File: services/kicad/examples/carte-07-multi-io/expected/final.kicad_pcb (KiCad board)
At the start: 2 copper layers, 115 x 85 mm, 47 parts, among them J1 IN_5V, J2 SWD, J3 IO0, J4 IO1, J5 IO2, J6 IO3, U1 STM32F103C8T6, U2 AMS1117-3.3

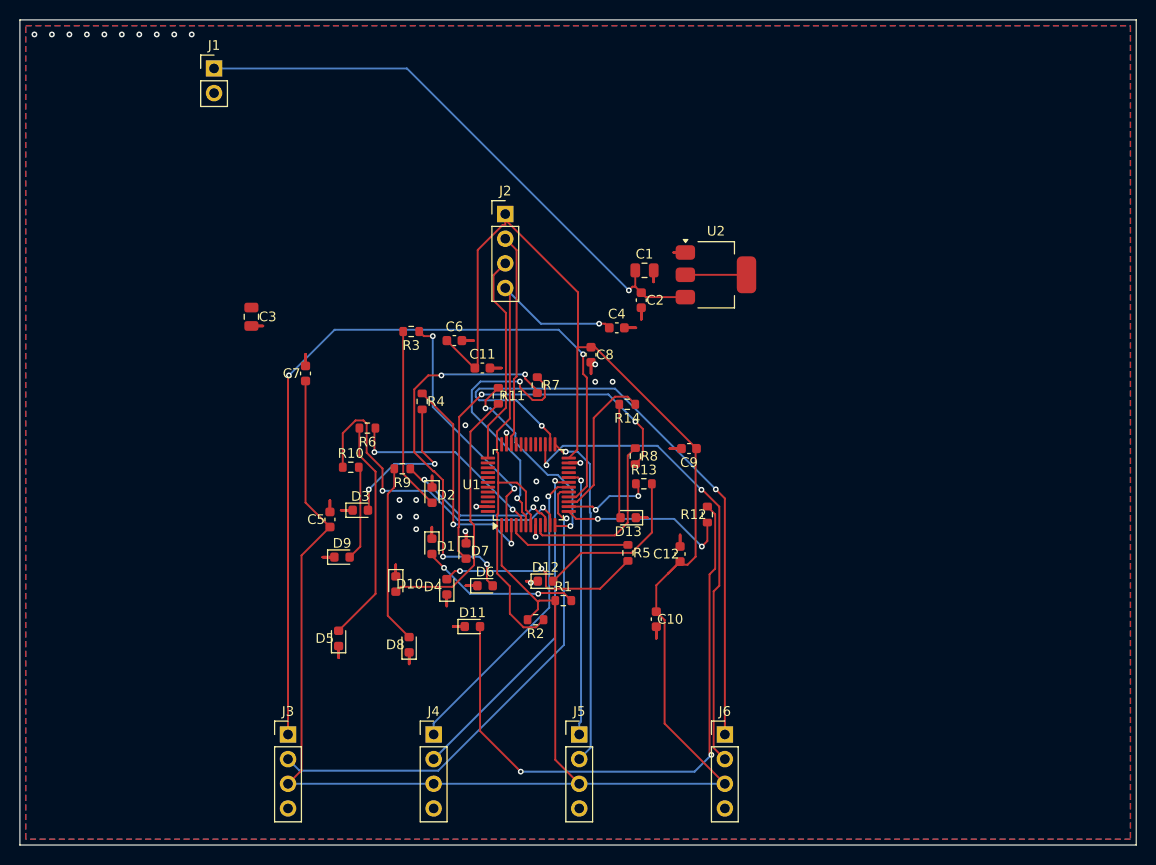
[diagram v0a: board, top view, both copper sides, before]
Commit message: test(examples): la carte 07 passe, et sa lenteur etait un tirage, pas sa taille
Elle est desormais routee a 100 %, zero connexion manquante, zero erreur de
severite `error` sur le board livre. 350 segments, 75 vias, deux couches.

Ce qui l a debloquee est le constat le plus instructif du banc.

Sa premiere version etait la carte-08 AMPUTEE de quatre paires de LED. Son
schema etait sain — verifie : aucune broche pointant vers un composant absent,
aucun composant isole, la meme structure que la carte dont elle derivait. Et
pourtant son PLACEMENT durait 1560 s, puis 70 minutes au tirage suivant, contre
104 s pour la carte-08 (56 composants) et 130 s pour la carte-10 (70). Douze a
trente fois plus long pour MOINS de composants.

J ai d abord soupconne une contention : une JVM Freerouting a 211 % de
processeur depuis sept heures, des travaux abandonnes par mes propres runs tues.
Mesure : 12 processeurs, charge moyenne 4,00, liste des sessions vide. Ce
n etait pas ca. C est le placement lui-meme, qui n a PAS de graine fixe.

Ce depot documentait deja la dispersion du placement en QUALITE — 6, 8 et 12
connexions manquantes selon le tirage. On mesure ici qu elle porte aussi sur la
DUREE, dans un rapport de trente. La duree d un pipeline ne se deduit donc pas
du nombre de composants, et un budget client calibre sur une moyenne coupera
certaines cartes en plein travail.

La carte a ete refaite en ETENDANT la carte-06, qui passe, au lieu de mutiler
la carte-08. Le placement est retombe a 662 s du premier coup, et il a fallu
deux tirages pour atteindre zero erreur — le routage est stochastique lui aussi.

Constat annexe, consigne dans docs/DECISIONS.md en attente de validation :
cinq travaux Freerouting ont tourne 996 passes chacun avec un score et un
nombre de connexions manquantes IDENTIQUES d un bout a l autre. Vingt minutes
par travail, entierement perdues, multipliees par les trois tirages de chaque
palier. Le levier serait d arreter sur absence de progression plutot que s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
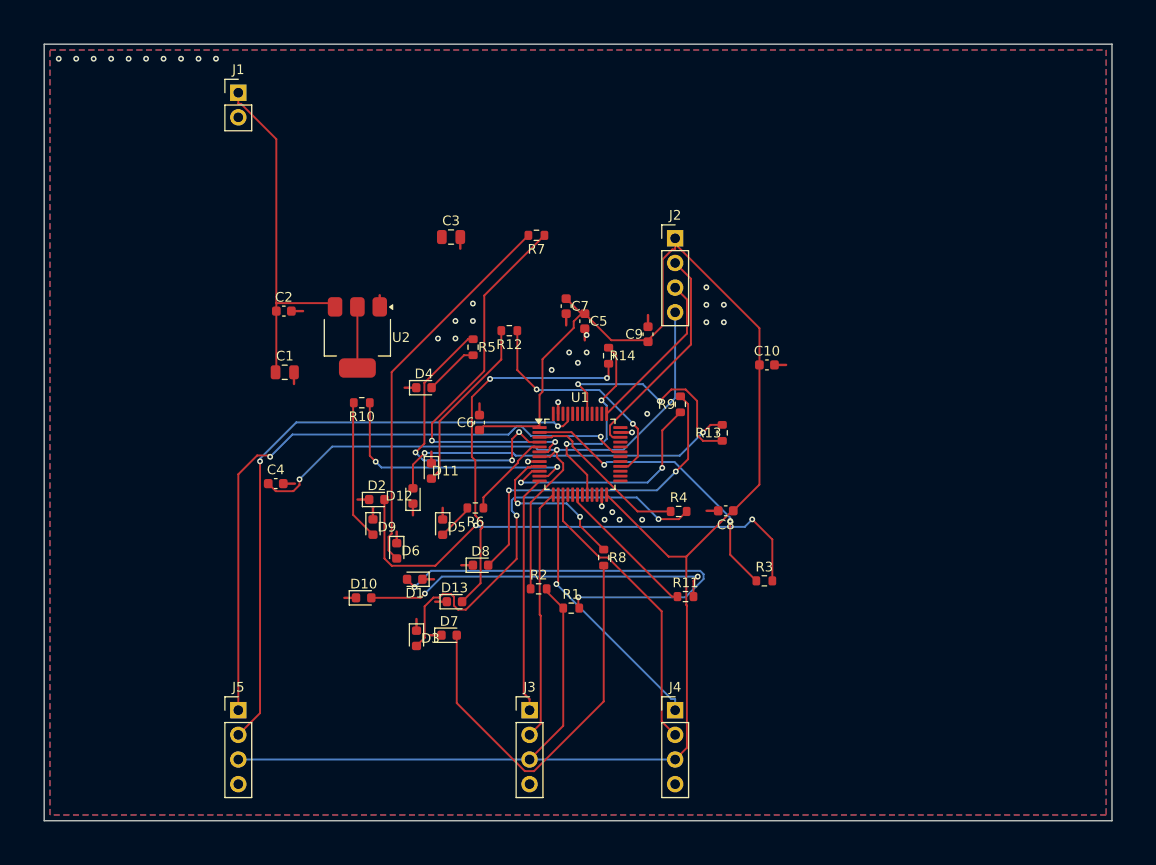
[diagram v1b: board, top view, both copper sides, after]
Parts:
- removed C11, C12: 100nF, C_0603_1608Metric
- removed J6: IO3, PinHeader_1x04_P2.54mm_Vertical
- moved R3 44.5 mm to (167.7, 120.3), turned to 0 degrees
- moved C4 38.6 mm to (117.4, 110.3)
- moved C1 38.5 mm to (118.3, 98.8)
- moved U2 37.5 mm to (125.8, 95.2), turned to -90 degrees
- moved C2 36.8 mm to (118.2, 92.5), turned to 0 degrees
- moved J5 35.2 mm to (113.5, 133.6)
- moved C5 33.3 mm to (149.2, 93.5), turned to -90 degrees
- moved R9 29.4 mm to (159.0, 102.1), turned to 90 degrees
- moved R4 28.7 mm to (158.9, 113.1), turned to 0 degrees
- moved C10 28.6 mm to (168.0, 98.0), turned to 0 degrees
- moved R11 28.3 mm to (159.6, 121.9), turned to 0 degrees
- moved R12 27.8 mm to (141.4, 94.5), turned to 180 degrees
- moved C7 27.7 mm to (147.3, 92.0), turned to -90 degrees
- moved R5 26.5 mm to (137.7, 96.2)
- moved J3 25.0 mm to (143.5, 133.6)
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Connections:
- U1 pad 12: IO_L8 -> EXT0_1
- U1 pad 13: IO_L9 -> EXT0_2
- U1 pad 14: IO_L10 -> EXT1_1
- U1 pad 15: IO_L11 -> EXT1_2
- U1 pad 16: EXT0_1 -> Net-(U1-16)
- U1 pad 17: EXT0_2 -> Net-(U1-17)
- U1 pad 18: EXT1_1 -> IO_L8
- U1 pad 19: EXT1_2 -> Net-(U1-19)
- U1 pad 20: EXT2_1 -> IO_L11
- U1 pad 25: EXT2_2 -> Net-(U1-25)
- U1 pad 26: EXT3_1 -> Net-(U1-26)
- U1 pad 27: EXT3_2 -> Net-(U1-27)
- U1 pad 28: Net-(U1-28) -> IO_L9
- U1 pad 31: Net-(U1-31) -> EXT2_1
- U1 pad 41: Net-(U1-41) -> IO_L10
- U1 pad 45: Net-(U1-45) -> EXT2_2
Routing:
- net GND: track 108.0 -> 33.6 mm, vias 27 -> 34
- net EXT3_1: track 65.6 -> 0.00 mm, vias 2 -> 0
- net EXT0_1: track 86.4 -> 24.5 mm, vias 2 -> 0
- net +3V3: track 230.3 -> 178.1 mm
- net EXT3_2: track 50.3 -> 0.00 mm, vias 2 -> 0
- net LEDA9: track 63.3 -> 18.2 mm, vias 2 -> 0
- net EXT2_1: track 27.6 -> 67.1 mm, vias 1 -> 2
- net LEDA0: track 18.9 -> 53.6 mm, vias 0 -> 2
- net LED_PWR: track 16.5 -> 47.1 mm
- net EXT2_2: track 35.3 -> 63.8 mm, vias 1 -> 2
- net LEDA1: track 16.2 -> 43.4 mm
- net LEDA11: track 11.7 -> 38.7 mm, vias 0 -> 2
- net EXT0_2: track 51.7 -> 25.8 mm, vias 1 -> 0
- net VIN: track 60.3 -> 36.8 mm, vias 1 -> 0
- net LEDA3: track 23.1 -> 3.82 mm
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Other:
- board size 115 x 85 mm -> 110 x 80 mm

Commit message: feat(kicad): placement pro et routage 100 % fabricable sur les 16 cartes -- integration sur main (#164)
Branche d'integration coupee depuis origin/main (fab2a82, PR #162) : les
fichiers cles de main etaient des instantanes de feat/placement-seed-snap-
bypass (routing.py = 7981019, placement.py = 437a8b4...). On reprend donc
l'arbre entier de cette branche (345 commits, dernier 9f48667) et on y
conserve ce que main seul apportait :
- tools/verrou_routage.py + son test : « 6,2 Go par routage » rectifie
  (0,2 Go mesure ; c'est la concurrence qui emballe la memoire) ;
- tests/test_driver_llm_resync.py ;
- CLAUDE.md, PLAN.md, DECISIONS.md : fusion a trois voies, les sections
  des deux lignes conservees (2026-09-05 conteneur/verrou, 2026-09-07
  parcours asynchrone et chaine du driver, 2026-09-09/10 lecons).
Les skills *-delegate restent supprimes (remplaces le 2026-08-30).

Contenu : banc en deux phases (placement valide puis routage gele), snap
sur les regles natives, repli GND cible, journal Freerouting incremental,
horloge sans progres, via d'echappement vers le plan principal,
serigraphie degagee ; 16 cartes livrees a 100 %, 0 erreur DRC.

Verification : pytest services/kicad 1805 passed, 16 skipped ;
pnpm type-check 8/8.


Claude-Session: https://claude.ai/code/session_01TnMqm4La2CxQHHB5K8aSSV

Co-authored-by: Claude Fable 5.1 <noreply@anthropic.com>
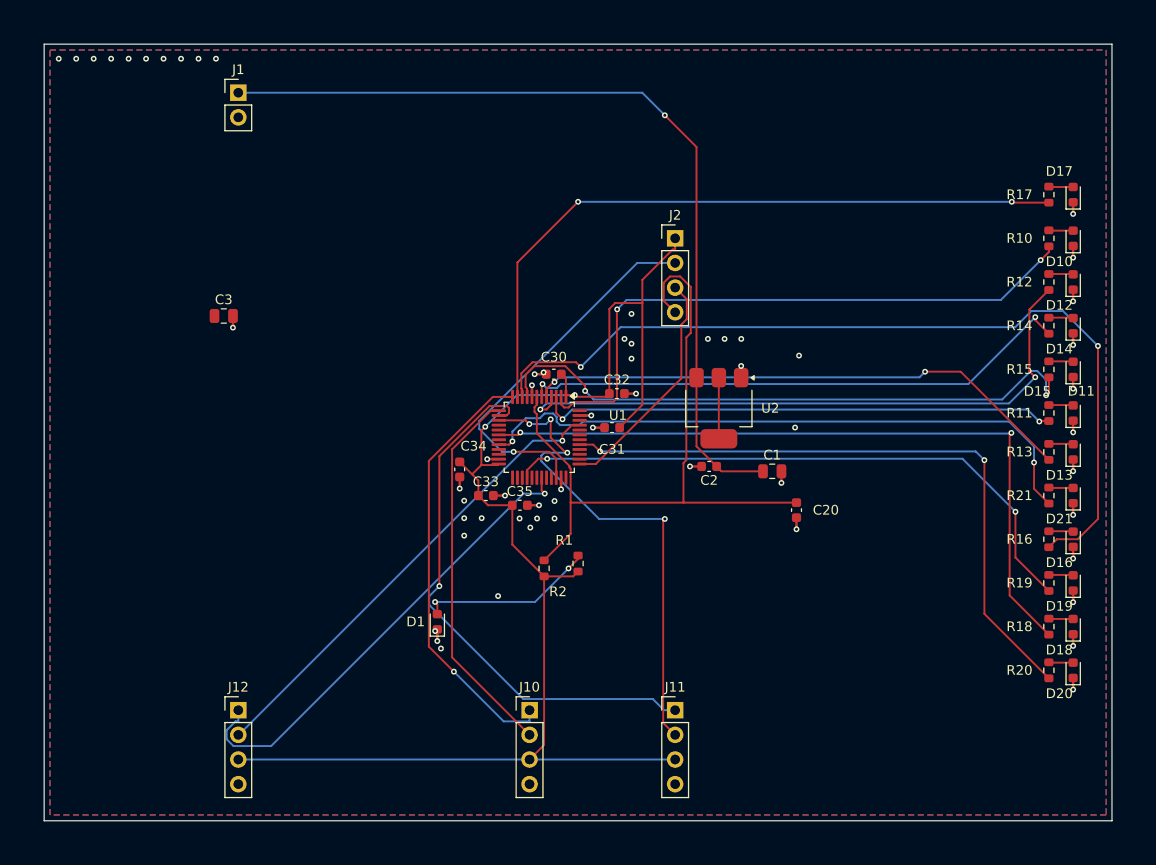
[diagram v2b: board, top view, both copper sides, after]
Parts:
- removed C10, C4, C5, C6, C7, C8, C9: 100nF, C_0603_1608Metric
- removed D2, D3, D4, D5, D6, D7, D8, D9: LED, LED_0603_1608Metric
- removed J3: IO0, PinHeader_1x04_P2.54mm_Vertical
- removed J4: IO1, PinHeader_1x04_P2.54mm_Vertical
- removed J5: IO2, PinHeader_1x04_P2.54mm_Vertical
- removed R3, R4, R5, R6, R7, R8, R9: 1k, R_0603_1608Metric
- added C20: 100nF, C_0603_1608Metric, F.Cu at (171.0, 113.0)
- added C30: 100nF, C_0603_1608Metric, F.Cu at (146.0, 99.0)
- added C31: 100nF, C_0603_1608Metric, F.Cu at (152.0, 104.5)
- added C32: 100nF, C_0603_1608Metric, F.Cu at (152.5, 101.0)
- added C33: 100nF, C_0603_1608Metric, F.Cu at (139.0, 111.5)
- added C34: 100nF, C_0603_1608Metric, F.Cu at (136.3, 108.8)
- added C35: 100nF, C_0603_1608Metric, F.Cu at (142.5, 112.5)
- added D14: LED, LED_0603_1608Metric, F.Cu at (199.5, 94.0)
- added D15: LED, LED_0603_1608Metric, F.Cu at (199.5, 98.5)
- added D16: LED, LED_0603_1608Metric, F.Cu at (199.5, 116.0)
- added D17: LED, LED_0603_1608Metric, F.Cu at (199.5, 80.5)
- added D18: LED, LED_0603_1608Metric, F.Cu at (199.5, 125.0)
- added D19: LED, LED_0603_1608Metric, F.Cu at (199.5, 120.5)
- added D20: LED, LED_0603_1608Metric, F.Cu at (199.5, 129.5)
- added D21: LED, LED_0603_1608Metric, F.Cu at (199.5, 111.5)
- added J10: IO0, PinHeader_1x04_P2.54mm_Vertical, F.Cu at (143.5, 133.6)
- added J11: IO1, PinHeader_1x04_P2.54mm_Vertical, F.Cu at (158.5, 133.6)
- added J12: IO2, PinHeader_1x04_P2.54mm_Vertical, F.Cu at (113.5, 133.6)
- added R15: 1k, R_0603_1608Metric, F.Cu at (197.0, 98.5)
- added R16: 1k, R_0603_1608Metric, F.Cu at (197.0, 116.0)
- added R17: 1k, R_0603_1608Metric, F.Cu at (197.0, 80.5)
- added R18: 1k, R_0603_1608Metric, F.Cu at (197.0, 125.0)
- added R19: 1k, R_0603_1608Metric, F.Cu at (197.0, 120.5)
- added R20: 1k, R_0603_1608Metric, F.Cu at (197.0, 129.5)
- added R21: 1k, R_0603_1608Metric, F.Cu at (197.0, 111.5)
- moved D10 81.9 mm to (199.5, 85.0), turned to 90 degrees
- moved R10 72.8 mm to (197.0, 85.0), turned to 90 degrees
- moved D12 71.5 mm to (199.5, 89.5)
- moved D11 66.4 mm to (199.5, 103.0), turned to 90 degrees
- moved D13 65.6 mm to (199.5, 107.0), turned to 90 degrees
- moved R12 55.8 mm to (197.0, 89.5), turned to 90 degrees
- moved C1 51.2 mm to (168.5, 109.0)
- moved C2 46.6 mm to (162.0, 108.5), turned to 180 degrees
- moved R14 45.5 mm to (197.0, 94.0), turned to 90 degrees
- moved R11 41.9 mm to (197.0, 103.0), turned to 90 degrees
- moved U2 37.9 mm to (163.0, 102.5)
- moved R13 33.7 mm to (197.0, 107.0)
- moved C3 24.8 mm to (112.0, 93.0)
- moved D1 4.96 mm to (134.0, 124.5), turned to 90 degrees
- moved R1 4.65 mm to (148.5, 118.5), turned to 90 degrees
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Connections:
- D10 pad 2: LEDA8 -> LEDA0
- D11 pad 2: LEDA9 -> LEDA1
- D12 pad 2: LEDA10 -> LEDA2
- D13 pad 2: LEDA11 -> LEDA3
- R10 pad 1: IO_L7 -> IO_L0
- R10 pad 2: LEDA7 -> LEDA0
- R11 pad 1: IO_L8 -> IO_L1
- R11 pad 2: LEDA8 -> LEDA1
- R12 pad 1: IO_L9 -> IO_L2
- R12 pad 2: LEDA9 -> LEDA2
- R13 pad 1: IO_L10 -> IO_L3
- R13 pad 2: LEDA10 -> LEDA3
- R14 pad 1: IO_L11 -> IO_L4
- R14 pad 2: LEDA11 -> LEDA4
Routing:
- net IO_L6: track 24.1 -> 90.5 mm
- net IO_L8: track 15.1 -> 75.5 mm, vias 0 -> 2
- net VIN: track 36.8 -> 88.3 mm, vias 0 -> 1
- net LEDA0: track 53.6 -> 2.52 mm, vias 2 -> 0
- net IO_L3: track 9.14 -> 57.1 mm, vias 0 -> 2
- net IO_L5: track 17.0 -> 63.2 mm
- net IO_L11: track 21.0 -> 65.6 mm
- net IO_L10: track 23.8 -> 67.6 mm
- net IO_L7: track 27.5 -> 71.2 mm
- net LEDA1: track 43.4 -> 2.52 mm, vias 2 -> 0
- net LEDA5: track 42.0 -> 2.52 mm
- net IO_L9: track 24.1 -> 63.4 mm
- net LEDA4: track 39.6 -> 2.52 mm
- net IO_L1: track 17.1 -> 53.6 mm, vias 0 -> 2
- net LEDA11: track 38.7 -> 2.52 mm, vias 2 -> 0
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
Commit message: test(examples): quatre cartes livrées plus petites — contour resserré mesuré sur le banc (D-2026-09-13-c A)
Banc rejoué en taille heuristique (phase 1 puis phase 2 à placement gelé) :
carte-01 25x20 -> 24,8x17 (84 % de surface), carte-04 60x45 -> 45x44,8
(75 %), carte-06 80x60 -> 65,2x59,8 (81 %), carte-07 110x80 -> 99,5x79,8
(90 %) — toutes 100 % routées, 0 erreur DRC (vérifié en local), rendus 3D
régénérés. Gain nul sur les cartes denses (le génétique remplit la carte) ;
08 et 09 non livrées (dispersion du routage, surface inchangée) ; carte-11
non livrée (carte d'escalade). Tableau complet dans docs/DECISIONS.md.

Co-Authored-By: Claude Fable 5.1 <noreply@anthropic.com>
Claude-Session: https://claude.ai/code/session_01TnMqm4La2CxQHHB5K8aSSV
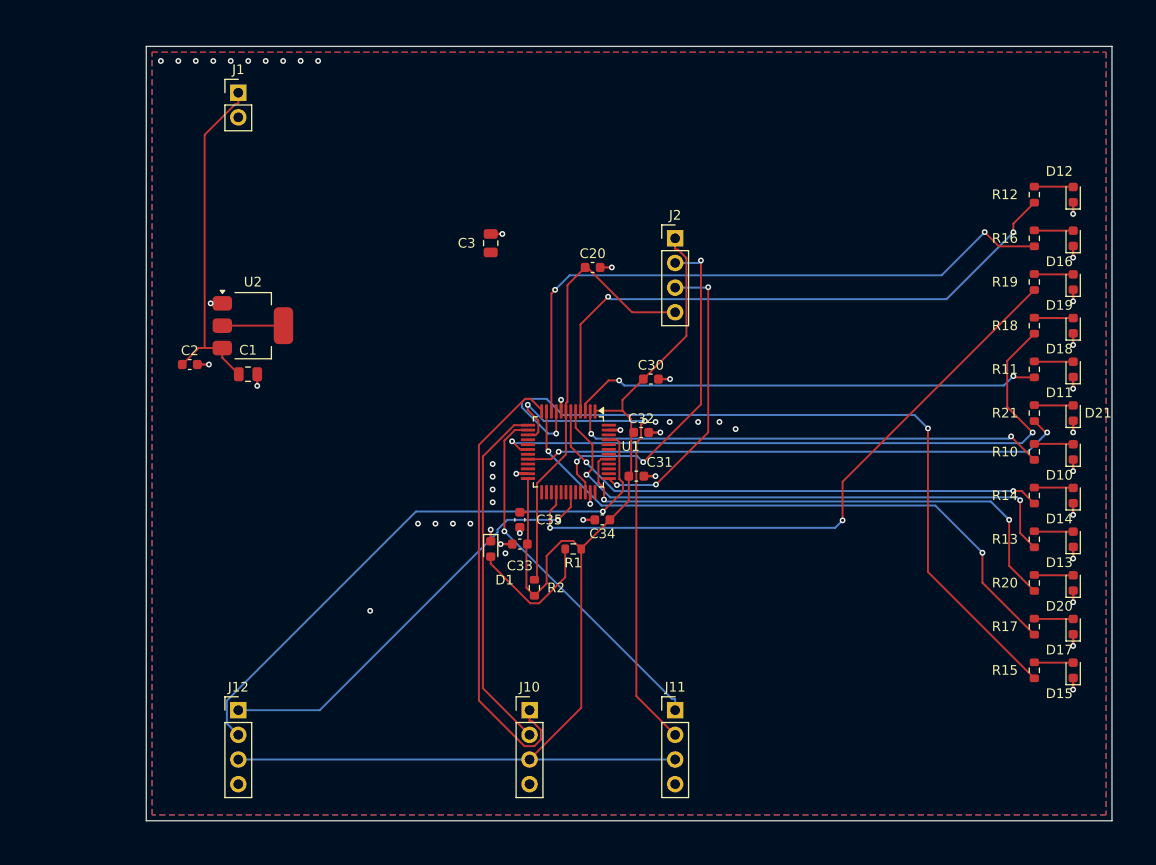
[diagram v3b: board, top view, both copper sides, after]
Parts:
- moved C1 54.9 mm to (114.5, 99.0)
- moved C2 54.5 mm to (108.5, 98.0), turned to 0 degrees
- moved U2 48.7 mm to (115.0, 94.0), turned to 0 degrees
- moved R17 44.5 mm to (195.5, 125.0)
- moved D17 44.5 mm to (199.5, 125.0)
- moved C20 32.6 mm to (150.0, 88.0), turned to 0 degrees
- moved R15 31.0 mm to (195.5, 129.5)
- moved R16 31.0 mm to (195.5, 85.0)
- moved R18 31.0 mm to (195.5, 94.0)
- moved R19 31.0 mm to (195.5, 89.5)
- moved D15 31.0 mm to (199.5, 129.5)
- moved D16 31.0 mm to (199.5, 85.0)
- moved D18 31.0 mm to (199.5, 94.0)
- moved D19 31.0 mm to (199.5, 89.5)
- moved C3 28.5 mm to (139.5, 85.5), turned to 90 degrees
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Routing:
- net VIN: track 88.3 -> 36.1 mm, vias 1 -> 0
- net NRST: track 72.4 -> 45.5 mm
- net IO_L6: track 90.5 -> 65.1 mm
- net EXT1_1: track 56.6 -> 38.1 mm
- net IO_L5: track 63.2 -> 81.0 mm
- net IO_L0: track 63.7 -> 49.3 mm
- net +3V3: track 144.5 -> 132.4 mm, vias 2 -> 0
- net EXT2_2: track 48.7 -> 60.2 mm
- net IO_L10: track 67.6 -> 56.3 mm
- net IO_L11: track 65.6 -> 56.4 mm
- net IO_L7: track 71.2 -> 63.9 mm
- net IO_L8: track 75.5 -> 68.6 mm
- net SWCLK: track 24.2 -> 31.1 mm, vias 0 -> 3
- net IO_L1: track 53.6 -> 48.7 mm
- net EXT2_1: track 49.2 -> 44.6 mm
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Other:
- board size 110 x 80 mm -> 99.5 x 79.8 mm
